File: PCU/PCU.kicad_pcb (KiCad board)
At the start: 4 copper layers, 140 x 140 mm, 760 parts, among them IC1 TCAN3403DDFRQ1, IC10 LM321LVIDBVR, IC11 LM321LVIDBVR, IC12 STM32G473CCT3, IC13 TCAN3403DDFRQ1, IC14 UCC27211DR, IC15 UCC27211DR, IC16 UCC27211DR, IC17 LM321LVIDBVR, IC18 LM321LVIDBVR, IC19 LM321LVIDBVR, IC2 UCC27211DR, IC20 STM32G473CCT3, IC21 TCAN3403DDFRQ1, IC22 UCC27211DR, IC23 UCC27211DR, IC24 UCC27211DR, IC25 LM321LVIDBVR, IC26 LM321LVIDBVR, IC27 LM321LVIDBVR, IC28 STM32G473CCT3, IC29 AP63203WU-7, IC3 UCC27211DR, IC30 STM32G473CCT3, IC31 LM321LVIDBVR, IC32 LM5060MMX_NOPB, IC33 LM321LVIDBVR, IC34 AP63205WU-7, IC35 AP63203WU-7, IC36 TCAN3403DDFRQ1, IC37 LM321LVIDBVR, IC38 STM32G473CCT3, IC4 UCC27211DR, IC5 TCAN3403DDFRQ1, IC6 UCC27211DR, IC7 UCC27211DR, IC8 UCC27211DR, IC9 LM321LVIDBVR, J1 XT60PW-M, J10 JST SH 5Pin, J11 JST SH 3Pin, J12 JST SH 5Pin, J13 JST SH 3Pin, J14 JST SH 5Pin, J15 JST SH 3Pin, J16 B2B-PH-K-S, J17 B2B-PH-K-S, J18 B2B-PH-K-S, J19 JST SH 5Pin, J2 B4B-PH-K-S_LF__SN_, J20 JST SH 3Pin, J21 USB4120-03-C, J3 B4B-PH-K-S_LF__SN_, J4 Conn_01x03_Pin, J5 Conn_01x03_Pin, J6 Conn_01x03_Pin, J7 Conn_01x03_Pin, J8 JST SH 5Pin, J9 JST SH 3Pin, Q1 SQJA06EP-T1_GE3, Q10 SQJA06EP-T1_GE3, Q11 SQJA06EP-T1_GE3, Q12 SQJA06EP-T1_GE3, Q13 SQJA06EP-T1_GE3, Q14 SQJA06EP-T1_GE3, Q15 SQJA06EP-T1_GE3, Q16 SQJA06EP-T1_GE3, Q17 SQJA06EP-T1_GE3, Q18 SQJA06EP-T1_GE3, Q19 SQJA06EP-T1_GE3, Q2 SQJA06EP-T1_GE3, Q20 SQJA06EP-T1_GE3, Q21 BC846B, Q22 DMP6023LFG-7, Q23 NTMFS5H600NLT1G, Q24 NTMFS5H600NLT1G, Q25 NTMFS5H600NLT1G, Q26 NTMFS5H600NLT1G, Q27 BC846B, Q28 SQJA06EP-T1_GE3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

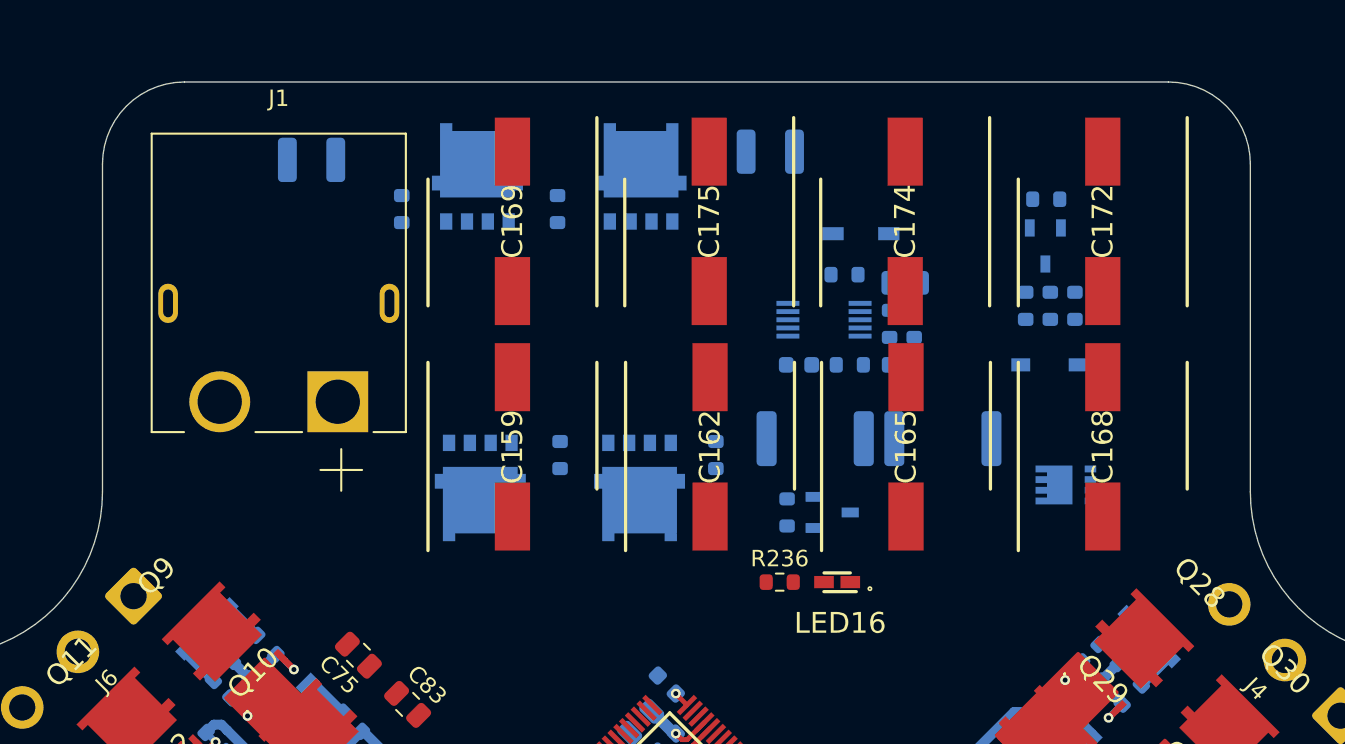
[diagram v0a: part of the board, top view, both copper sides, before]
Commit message: Precharge Block Routed
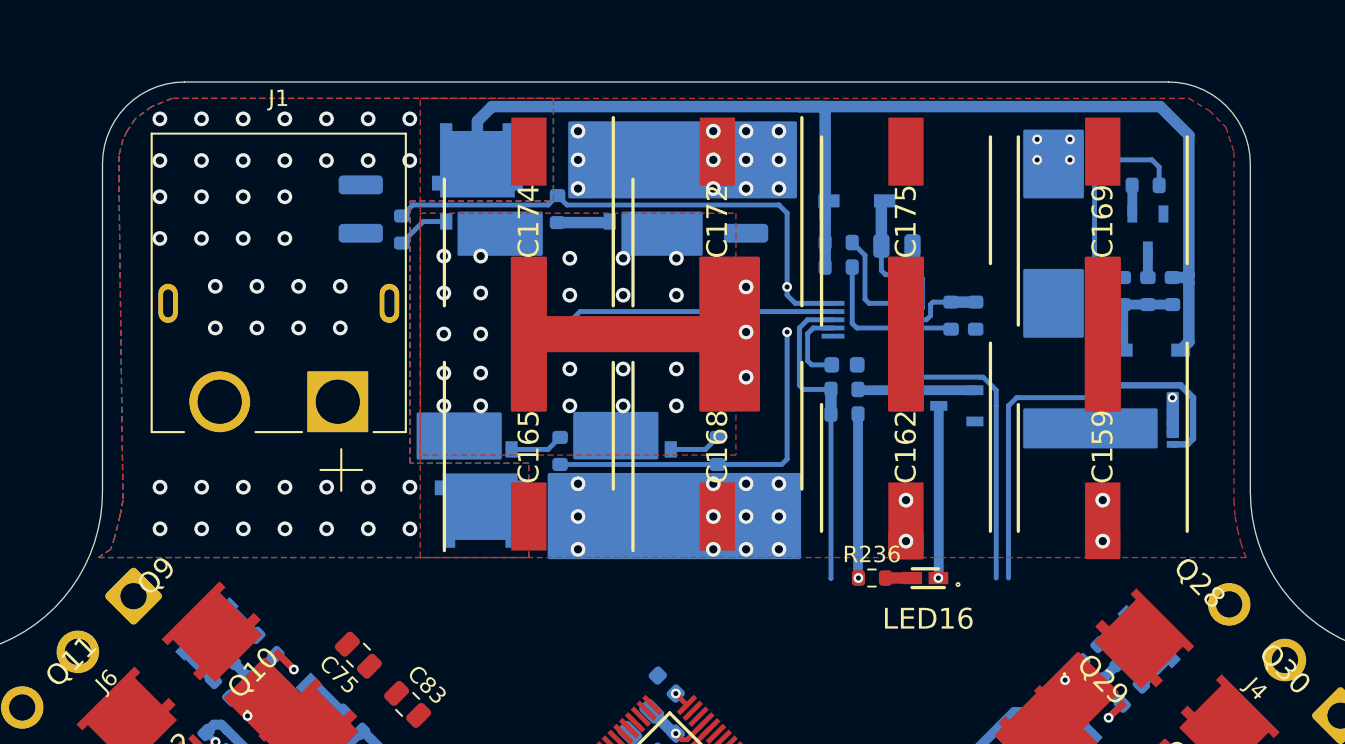
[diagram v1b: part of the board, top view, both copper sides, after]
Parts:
- moved C159 36.0 mm to (163.5, 41.2), turned to -90 degrees
- moved C169 36.0 mm to (163.5, 27.5), turned to 90 degrees
- moved C168 23.5 mm to (140.0, 41.2)
- moved C172 23.5 mm to (140.0, 27.5)
- moved C165 23.0 mm to (128.5, 41.2)
- moved C174 22.9 mm to (128.5, 27.5)
- moved R230 19.2 mm to (160.5, 28.2), turned to 90 degrees
- moved C175 12.0 mm to (151.5, 27.5), turned to 90 degrees
- moved C162 11.9 mm to (151.5, 41.2), turned to -90 degrees
- moved Q27 10.0 mm to (154.6, 38.8), turned to 180 degrees
- moved R235 8.28 mm to (147.8, 37.8), turned to 0 degrees
- moved R229 7.85 mm to (160.5, 36.8), turned to 90 degrees
- moved R214 7.10 mm to (147.4, 30.3)
- moved Z1 6.31 mm to (166.5, 35.4)
- moved Q21 6.31 mm to (166.2, 28.1)
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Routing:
- net /+Vbat: track 0.00 -> 73.9 mm, vias 0 -> 45
- net /Active Precharge/gate: track 0.00 -> 56.9 mm, vias 0 -> 2
- net /Active Precharge/EN_Precharge: track 0.00 -> 35.1 mm
- net /Active Precharge/EN_mainBus: track 0.00 -> 19.7 mm
- net /Active Precharge/mainBus_nFault: track 0.00 -> 19.3 mm
- net /Active Precharge/com_source: track 0.00 -> 17.2 mm, vias 0 -> 22
- net Net-(Q22-G): track 0.00 -> 16.5 mm
- net Net-(LED16-K): track 0.00 -> 10.5 mm, vias 0 -> 1
- net +3.3V_Logic: track 14.4 -> 24.5 mm, vias 5 -> 6
- net Net-(D44-K): track 0.00 -> 9.96 mm
- net Net-(IC32-UVLO): track 0.00 -> 9.61 mm
- net Net-(Q27-B): track 0.00 -> 7.15 mm
- net Net-(IC32-SENSE): track 0.00 -> 6.34 mm
- net Net-(Z1-A): track 0.00 -> 5.77 mm
- net Net-(IC32-OVP): track 0.00 -> 5.14 mm
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- added copper zone on F.Cu, net +Vbus
- added copper zone on B.Cu, net /+Vbat
- added copper zone on F.Cu, net /+Vbat
- added copper zone on F.Cu, net /Active Precharge/com_source

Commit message: PSU Blocks Routed
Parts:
- C157, C158, C160, C167, C170, C171, C173, C176, C177, C207, C208, C209, C213, C215, C218, C219, C221, C222, C226, C227, C229, D1, D38, D39, D40, D41, D47, D48, IC29, IC34, IC35, PS1, PS2, R189, R258: moved to B.Cu
- moved LED10 345.8 mm to (222.0, 93.7)
- moved LED11 345.8 mm to (222.0, 96.2)
- moved LED12 345.8 mm to (222.0, 98.7)
- moved R196 344.0 mm to (226.8, 93.6), turned to 180 degrees
- moved R197 337.9 mm to (226.6, 96.3)
- moved R198 337.9 mm to (226.6, 98.8)
- moved TP6 335.2 mm to (223.4, 72.0)
- moved TP4 333.5 mm to (223.4, 76.6)
- moved TP5 333.5 mm to (223.6, 81.2)
- moved IC29 317.4 mm to (192.4, 72.9), turned to 180 degrees
- moved C160 315.5 mm to (192.5, 69.3)
- moved C178 315.3 mm to (192.4, 80.4)
- moved D41 313.6 mm to (190.8, 96.4), turned to 180 degrees
- moved C180 311.9 mm to (190.8, 96.4), turned to 90 degrees
- moved C166 311.5 mm to (192.0, 102.0), turned to 180 degrees
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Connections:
- C219 pad 2: Net-(IC35-FB) -> +3.3V_Logic
- C222 pad 2: Net-(IC35-FB) -> +3.3V_Logic
- C229 pad 2: +3.3V_Logic -> +3.3V_Logic_filtered
- C230 pad 2: +3.3V_Logic -> +3.3V_Logic_filtered
- C232 pad 1: +3.3V_Logic -> +3.3V_Logic_filtered
- C239 pad 1: +3.3V_Logic -> +3.3V_Logic_filtered
- C241 pad 2: +3.3V_Logic -> +3.3V_Logic_filtered
- C243 pad 2: +3.3V_Logic -> +3.3V_Logic_filtered
- C244 pad 2: +3.3V_Logic -> +3.3V_Logic_filtered
- C245 pad 2: +3.3V_Logic -> +3.3V_Logic_filtered
- C246 pad 2: +3.3V_Logic -> +3.3V_Logic_filtered
- C247 pad 2: +3.3V_Logic -> +3.3V_Logic_filtered
- C249 pad 2: +3.3V_Logic -> +3.3V_Logic_filtered
- C252 pad 1: +3.3V_Logic -> +3.3V_Logic_filtered
- C254 pad 1: +3.3V_Logic -> +3.3V_Logic_filtered
- D47 pad 1: +3.3V_Logic -> +3.3V_Logic_filtered
- D48 pad 1: +3.3V_Logic -> +3.3V_Logic_filtered
- FB2 pad 1: Net-(IC35-FB) -> +3.3V_Logic
- IC35 pad 1: Net-(IC35-FB) -> +3.3V_Logic
- IC36 pad 3: +3.3V_Logic -> +3.3V_Logic_filtered
- IC36 pad 5: +3.3V_Logic -> +3.3V_Logic_filtered
- IC38 pad 20: +3.3V_Logic -> +3.3V_Logic_filtered
- IC38 pad 21: +3.3V_Logic -> +3.3V_Logic_filtered
- IC38 pad 24: +3.3V_Logic -> +3.3V_Logic_filtered
- IC38 pad 36: +3.3V_Logic -> +3.3V_Logic_filtered
- IC38 pad 48: +3.3V_Logic -> +3.3V_Logic_filtered
- J19 pad 1: +3.3V_Logic -> +3.3V_Logic_filtered
- J2 pad 1: +3.3V_Logic -> +3.3V_Logic_filtered
- J3 pad 1: +3.3V_Logic -> +3.3V_Logic_filtered
- L5 pad 2: Net-(IC35-FB) -> +3.3V_Logic
- R207 pad 1: +3.3V_Logic -> +3.3V_Logic_filtered
- R236 pad 1: +3.3V_Logic -> +3.3V_Logic_filtered
- R258 pad 1: +3.3V_Logic -> +3.3V_Logic_filtered
- R259 pad 2: +3.3V_Logic -> +3.3V_Logic_filtered
- R265 pad 1: +3.3V_Logic -> +3.3V_Logic_filtered
- R272 pad 1: +3.3V_Logic -> +3.3V_Logic_filtered
- R288 pad 1: +3.3V_Logic -> +3.3V_Logic_filtered
- TH5 pad 1: +3.3V_Logic -> +3.3V_Logic_filtered
- TP11 pad 1: +3.3V_Logic -> +3.3V_Logic_filtered
- TP9 pad 1: Net-(IC35-FB) -> +3.3V_Logic
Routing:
- net +3.3V_Logic_filtered: track 0.00 -> 28.9 mm, vias 0 -> 7
- net +3.3V_Digital: track 15.8 -> 29.0 mm, vias 12 -> 14
- net +5V_Logic: track 0.00 -> 12.5 mm, vias 0 -> 2
- net Net-(IC34-SW): track 0.00 -> 12.4 mm, vias 0 -> 1
- net +3.3V_Logic: track 24.5 -> 12.4 mm, vias 6 -> 2
- net Net-(IC35-SW): track 0.00 -> 11.0 mm, vias 0 -> 1
- net +12V_PWR: track 0.00 -> 10.9 mm, vias 0 -> 3
- net Net-(IC29-SW): track 0.00 -> 10.7 mm, vias 0 -> 1
- net +12V_Logic: track 0.00 -> 10.2 mm, vias 0 -> 3
- net /HIGH PSU/SW: track 0.00 -> 8.77 mm, vias 0 -> 1
- net /Logic PSU/SW: track 0.00 -> 8.17 mm, vias 0 -> 1
- net Net-(FB1-Pad2): track 0.00 -> 6.56 mm, vias 0 -> 1
- net +Vbus: track 0.00 -> 6.24 mm, vias 28 -> 30
- net Net-(PS1-FB): track 0.00 -> 4.62 mm, vias 0 -> 1
- net /Logic PSU/V12Logic_Mesure: track 0.00 -> 4.50 mm, vias 0 -> 1
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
